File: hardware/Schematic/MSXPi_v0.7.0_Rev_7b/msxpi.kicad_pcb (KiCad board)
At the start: 2 copper layers, 101 x 64.7 mm, 37 parts, among them IC1 LD1117, J1 ROM_SWITCH, U1 28C256

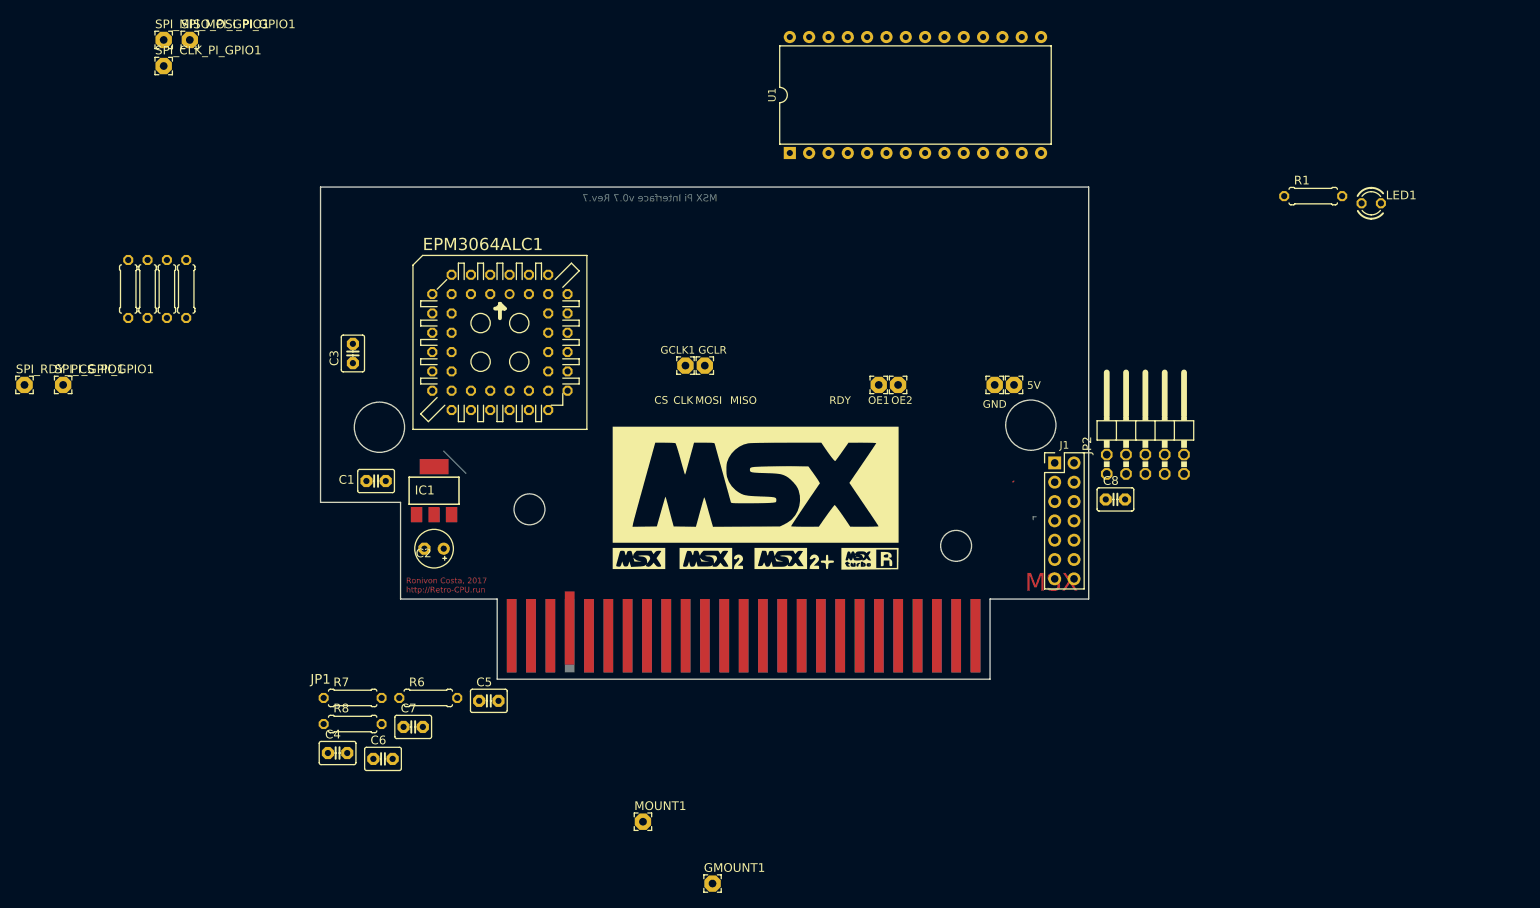
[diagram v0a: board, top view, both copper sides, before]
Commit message: Starting routing - before chnaging pin assigments support more clean routing traces
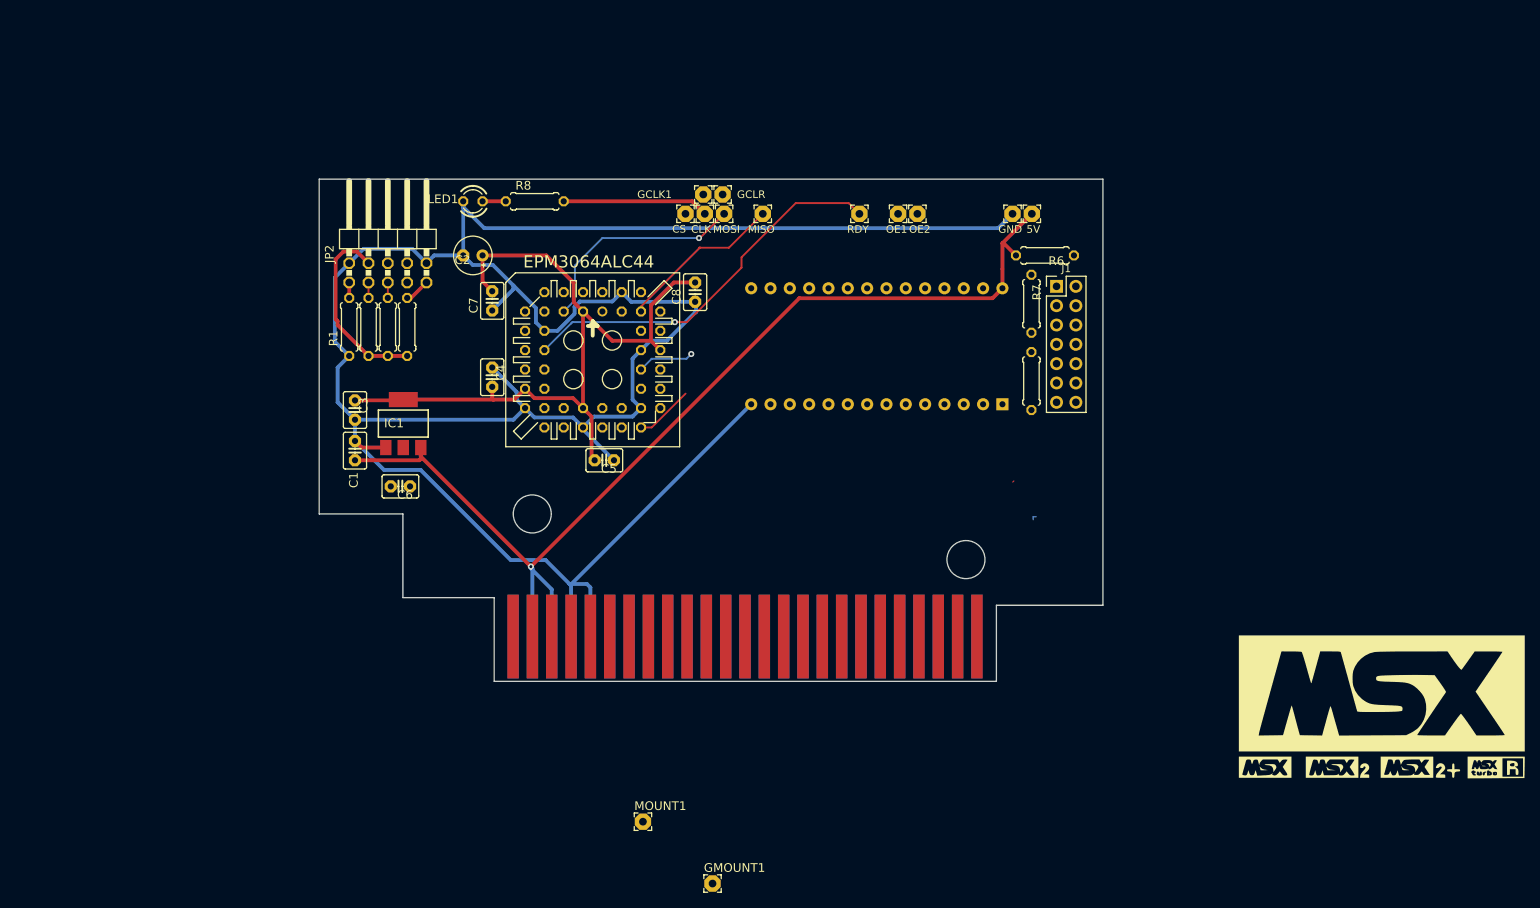
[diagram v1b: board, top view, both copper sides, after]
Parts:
- removed EPM3064ALC1: EPM3064S44, msxpi:PLCC-S44
- added EPM3064ALC44: EPM3064ALC44, msxpi:PLCC-S44, F.Cu at (134.1, 94.7)
- JP1: footprint msxpi:MSXCART -> Roni Footprints:MSX_CART
- R8: value R-US_0207/7 -> 470
- U1: moved to B.Cu
- moved R1 127.9 mm to (102.1, 90.4), turned to 90 degrees
- moved LED1 118.1 mm to (118.4, 73.9), turned to 180 degrees
- moved SPI_RDY_PI_GPIO1 112.0 mm to (169.2, 75.6)
- moved R5 111.7 mm to (191.8, 97.5)
- moved R7 103.2 mm to (191.8, 87.4), turned to -90 degrees
- moved JP2 102.7 mm to (107.2, 78.2)
- moved R6 99.8 mm to (193.5, 81.0), turned to 180 degrees
- moved G*** 86.7 mm to (237.7, 140.2)
- moved SPI_CS_PI_GPIO1 84.8 mm to (146.3, 75.6)
- moved SPI_MISO_PI_GPIO1 82.0 mm to (156.5, 75.6)
- moved SPI_MOSI_PI_GPIO1 73.8 mm to (151.4, 75.6)
- moved SPI_CLK_PI_GPIO1 73.7 mm to (148.8, 75.6)
- moved R8 72.7 mm to (126.5, 73.9)
- moved C8 61.6 mm to (147.6, 85.9), turned to 90 degrees
- moved JP1 60.7 mm to (147.8, 101.6)
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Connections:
- R8 pad 2: SPI_SCLK -> SPI_CLK
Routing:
- net GNDREF: track 0.37 -> 331.8 mm
- net +5V: track 4.46 -> 167.4 mm, vias 0 -> 1
- net +3.3V: track 0.00 -> 100.5 mm
- net SPI_RDY: track 0.00 -> 50.8 mm, vias 0 -> 1
- net SPI_MOSI: track 0.00 -> 29.1 mm, vias 0 -> 1
- net SPI_CLK: track 0.00 -> 26.7 mm, vias 0 -> 1
- net SPI_MISO: track 0.00 -> 21.8 mm
- net SPI_CS: track 0.00 -> 7.68 mm
- net TDI: track 0.00 -> 3.38 mm
- net Net-(LED1-PadA): track 0.00 -> 3.05 mm
- net TMS: track 0.00 -> 2.29 mm
- net TDO: track 0.00 -> 2.29 mm
- net TCK: track 0.00 -> 2.03 mm
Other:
- board size 101 x 64.7 mm -> 103 x 66 mm
- board text removed: "MSX"
- board text removed: "MSX Pi Interface v0.7 Rev.7"
- board text removed: "Ronivon Costa, 2017 http://Retro-CPU.run"

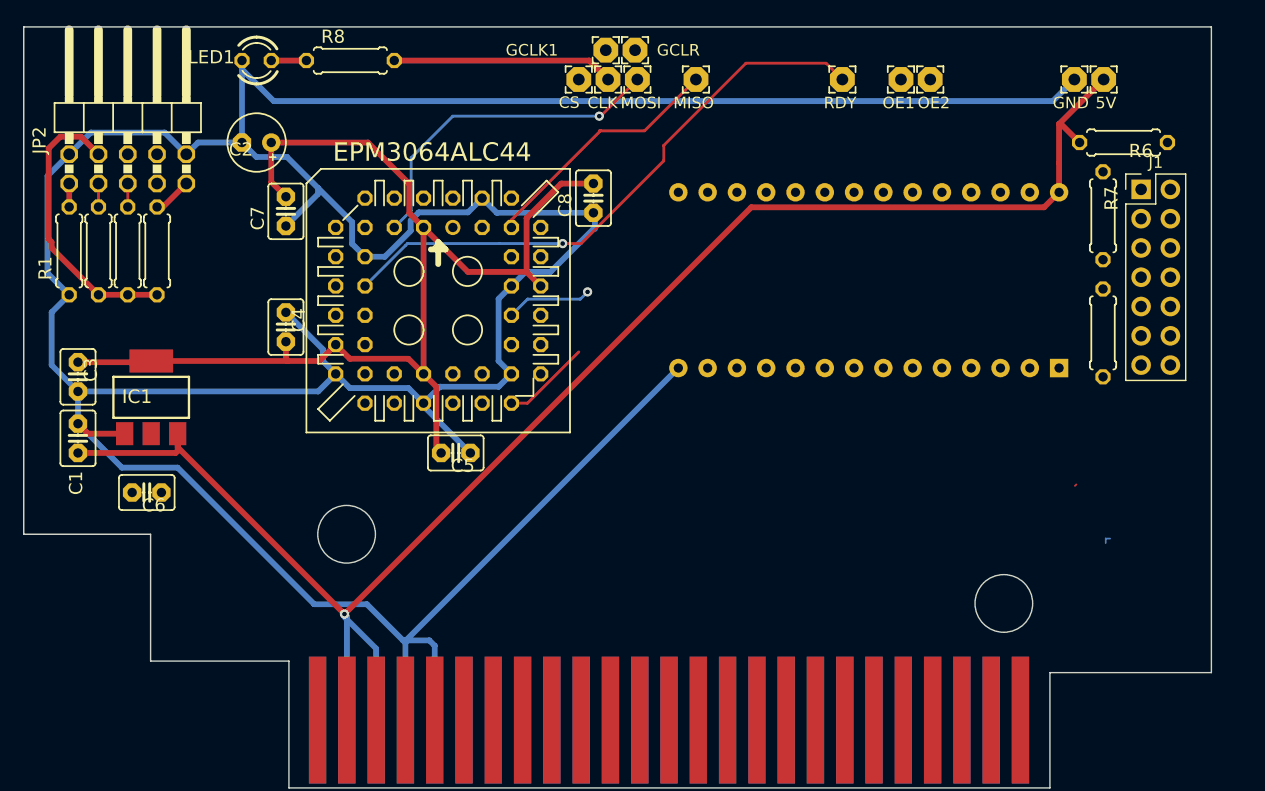
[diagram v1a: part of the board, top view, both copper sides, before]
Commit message: routing complete. need to update footprint for ld1117
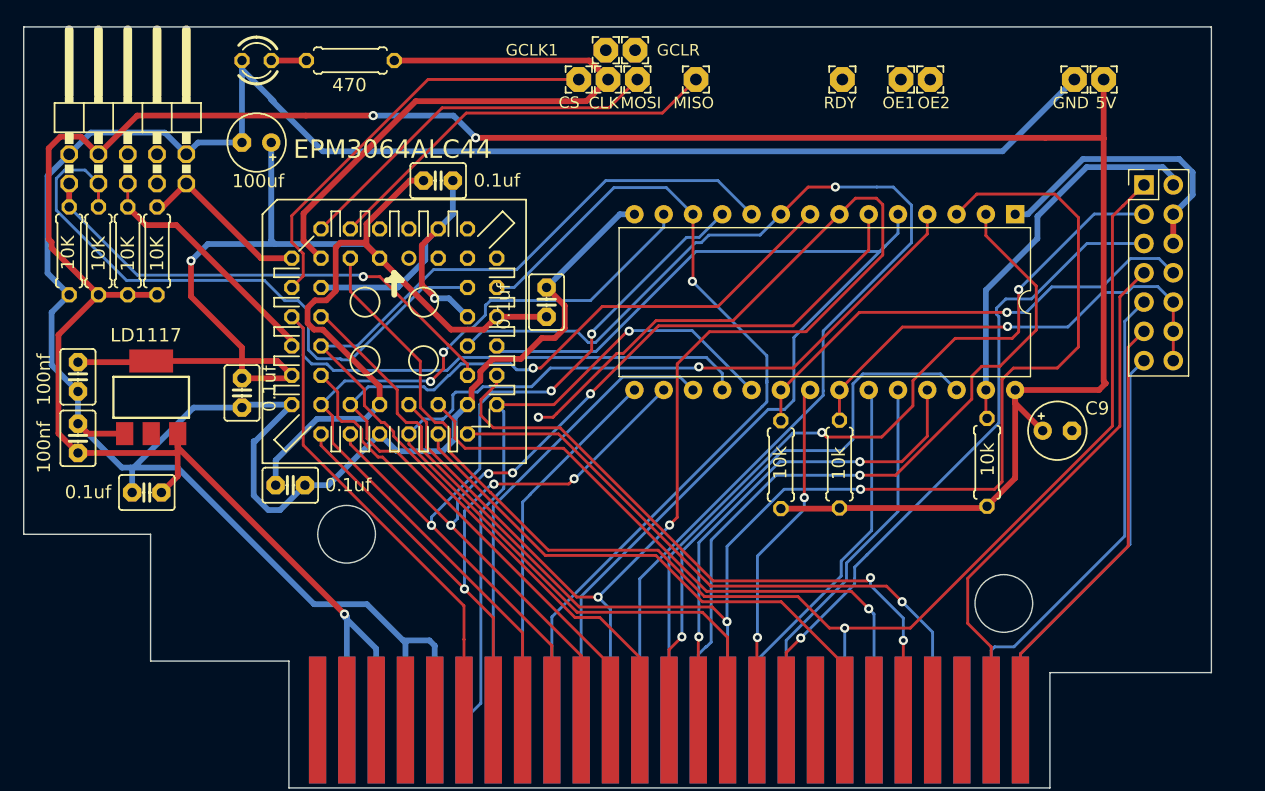
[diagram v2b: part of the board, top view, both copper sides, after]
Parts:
- added C9: 100uf, msxpi:E2,5-5, F.Cu at (187.8, 106.0)
- C4, C5, C6, C7, C8: value C2,5-3 -> 0.1uf
- U1: value 28C256 -> AT28C256; moved to F.Cu
- moved R6 37.2 mm to (168.9, 108.9), turned to -90 degrees
- moved C8 36.2 mm to (121.3, 110.7), turned to 180 degrees
- moved R7 35.3 mm to (163.8, 109.0)
- moved C7 23.9 mm to (143.5, 94.9), turned to -90 degrees
- moved C5 23.7 mm to (134.1, 84.3)
- moved R5 15.1 mm to (181.7, 108.8), turned to -90 degrees
- moved U1 13.9 mm to (184.2, 87.2), turned to -90 degrees
- moved C4 6.87 mm to (117.1, 102.7), turned to 90 degrees
- moved EPM3064ALC44 4.65 mm to (130.3, 97.4)
- moved J1 0.46 mm to (195.3, 84.7)
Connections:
- EPM3064ALC44 pad 1: GCLR -> unconnected-(EPM3064ALC44-Pad1)
- EPM3064ALC44 pad 11: D2 -> D6
- EPM3064ALC44 pad 12: SPI_RDY -> A7
- EPM3064ALC44 pad 14: D4 -> A0
- EPM3064ALC44 pad 16: D6 -> A4
- EPM3064ALC44 pad 18: D3 -> D4
- EPM3064ALC44 pad 19: D7 -> D2
- EPM3064ALC44 pad 2: OE2 -> unconnected-(EPM3064ALC44-Pad2)
- EPM3064ALC44 pad 20: D1 -> D0
- EPM3064ALC44 pad 21: D5 -> A2
- EPM3064ALC44 pad 24: A2 -> A6
- EPM3064ALC44 pad 25: A4 -> A3
- EPM3064ALC44 pad 26: A3 -> /RD
- EPM3064ALC44 pad 27: A5 -> /IORQ
- EPM3064ALC44 pad 28: SPI_CS -> /WAIT
- EPM3064ALC44 pad 29: A1 -> D7
- EPM3064ALC44 pad 31: A0 -> BUSDIR
- EPM3064ALC44 pad 33: A6 -> A5
- EPM3064ALC44 pad 34: SPI_CLK -> A1
- EPM3064ALC44 pad 37: /RD -> D1
- EPM3064ALC44 pad 39: /WR -> unconnected-(EPM3064ALC44-Pad39)
- EPM3064ALC44 pad 4: A7 -> SPI_MISO
- EPM3064ALC44 pad 40: /IORQ -> unconnected-(EPM3064ALC44-Pad40)
- EPM3064ALC44 pad 41: SPI_MISO -> unconnected-(EPM3064ALC44-Pad41)
- EPM3064ALC44 pad 43: GCLK1 -> unconnected-(EPM3064ALC44-Pad43)
- EPM3064ALC44 pad 44: OE1 -> unconnected-(EPM3064ALC44-Pad44)
- EPM3064ALC44 pad 5: SPI_MOSI -> /WR
- EPM3064ALC44 pad 6: /BUSDIR -> SPI_MOSI
- EPM3064ALC44 pad 8: /WAIT -> SPI_CLK
- EPM3064ALC44 pad 9: D0 -> SPI_CS
- J1 pad 1: /SLTSL -> /WR
- J1 pad 11: /CS12 -> /CS2
- J1 pad 13: /WR -> /CS1
- J1 pad 14: /MEM_WE -> /MEM_OE
- J1 pad 2: /MEM_CE -> /MEM_WE
- J1 pad 7: /CS1 -> /SLTSL
- J1 pad 8: /MEM_OE -> /MEM_CE
- J1 pad 9: /CS2 -> /CS12
- U1 pad 1: A14 -> MEM_A14
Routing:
- net A7: track 0.00 -> 130.0 mm, vias 0 -> 2
- net A3: track 0.00 -> 122.8 mm, vias 0 -> 3
- net /WR: track 0.00 -> 121.8 mm, vias 0 -> 1
- net A1: track 0.00 -> 100.1 mm, vias 0 -> 1
- net A6: track 0.00 -> 97.4 mm, vias 0 -> 1
- net A5: track 0.00 -> 93.8 mm
- net A4: track 0.00 -> 90.3 mm, vias 0 -> 4
- net A2: track 0.00 -> 90.1 mm, vias 0 -> 1
- net A0: track 0.00 -> 89.8 mm
- net +5V: track 167.4 -> 255.4 mm, vias 1 -> 3
- net D6: track 0.00 -> 84.3 mm
- net D1: track 0.00 -> 76.1 mm, vias 0 -> 1
- net D2: track 0.00 -> 73.2 mm, vias 0 -> 2
- net D0: track 0.00 -> 73.2 mm, vias 0 -> 3
- net A14: track 0.18 -> 71.4 mm, vias 0 -> 2
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
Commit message: Almost ready for fabrication. Need to add logo and credits
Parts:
- IC1: value LD1117 -> LD117A; footprint msxpi:SOT223 -> Package_TO_SOT_SMD:SOT-223-3_TabPin2
- JP2: footprint msxpi:2X05_90 -> Connector_PinHeader_2.54mm:PinHeader_2x05_P2.54mm_Vertical
- moved JP2 8.10 mm to (102.2, 84.6), turned to 90 degrees
- moved C5 0.15 mm to (134.1, 84.2)
- moved IC1 0.10 mm to (109.2, 103.0), turned to 90 degrees
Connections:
- IC1 pad 2: (no net) -> +3.3V
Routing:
- net A3: track 122.8 -> 89.4 mm, vias 3 -> 2
- net GNDREF: track 294.3 -> 326.8 mm, vias 1 -> 2
- net TDO: track 55.1 -> 39.2 mm, vias 0 -> 1
- net A2: track 90.1 -> 84.9 mm
- net +3.3V: track 125.4 -> 130.4 mm
- net A15: track 58.6 -> 61.1 mm
- net +5V: track 255.4 -> 256.7 mm, vias 3 -> 2
- net /MEM_WE: track 34.0 -> 35.1 mm
- net A14: track 71.4 -> 72.5 mm
- net A12: track 65.0 -> 65.9 mm
